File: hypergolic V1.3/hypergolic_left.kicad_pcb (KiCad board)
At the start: 2 copper layers, 118.3 x 87.7 mm, 25 parts, among them SW10 SW_Push, SW11 SW_Push, SW12 SW_Push, SW14 SW_Push, SW15 SW_Push, SW16 SW_Push, SW17 SW_Push, SW18 SW_Push, SW2 SW_Push, SW20 SW_Push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

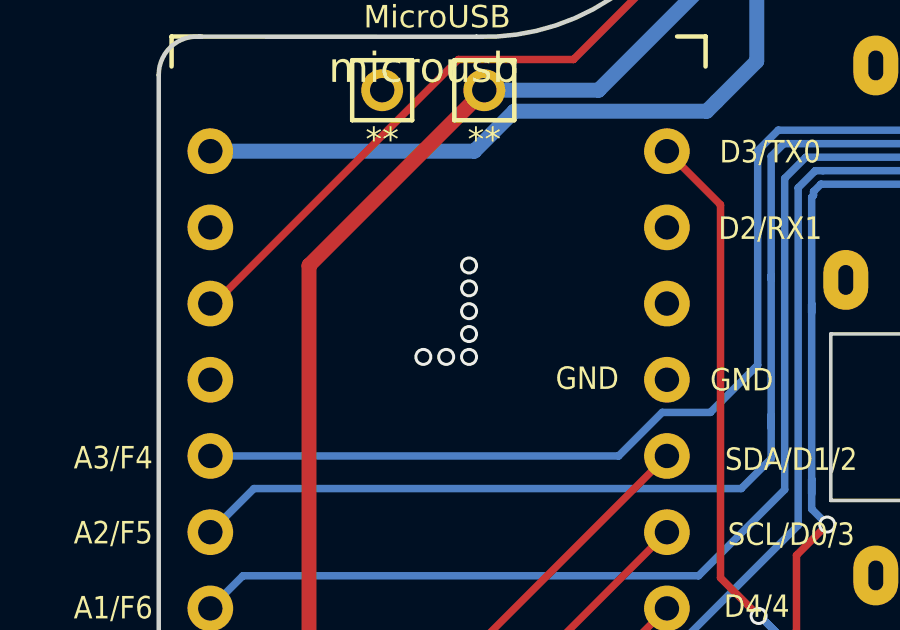
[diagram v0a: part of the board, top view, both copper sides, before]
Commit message: flip left power switch and add plate file
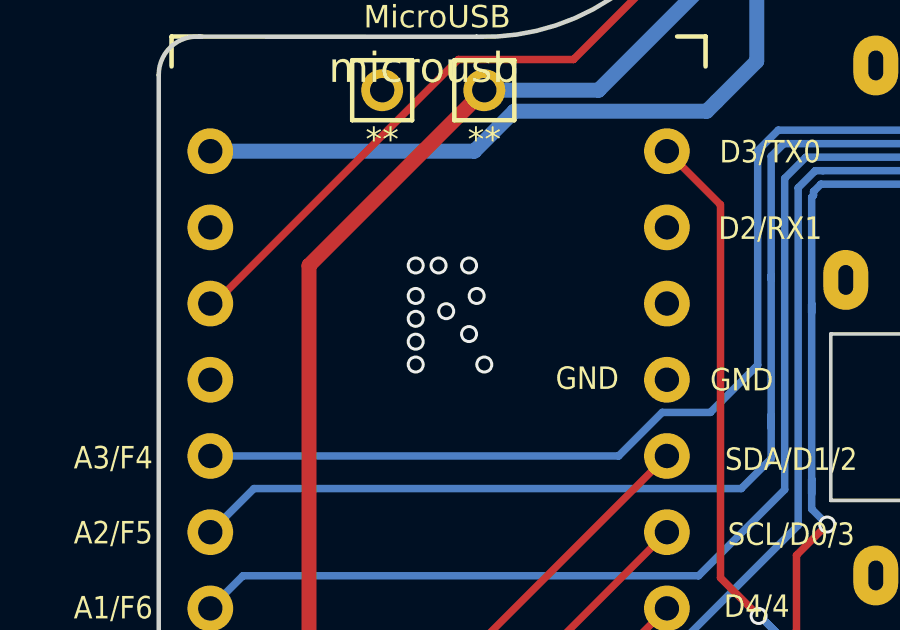
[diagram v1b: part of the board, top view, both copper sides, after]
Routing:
- net gnd: vias 7 -> 11
